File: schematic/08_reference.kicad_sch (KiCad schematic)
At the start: 20 parts, among them U501 OPA4192IDR

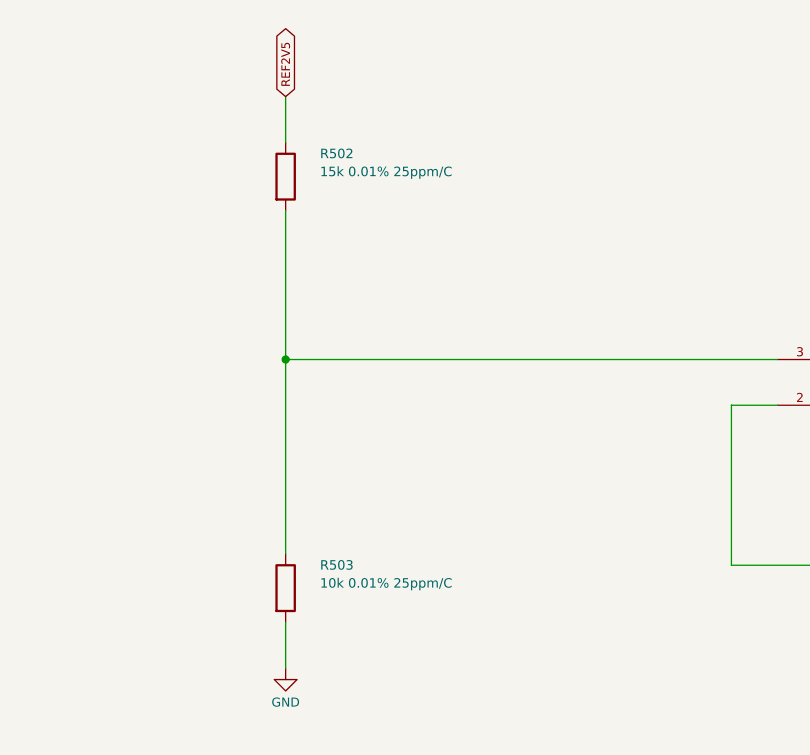
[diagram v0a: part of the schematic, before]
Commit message: add power supply, rail checks and parts list
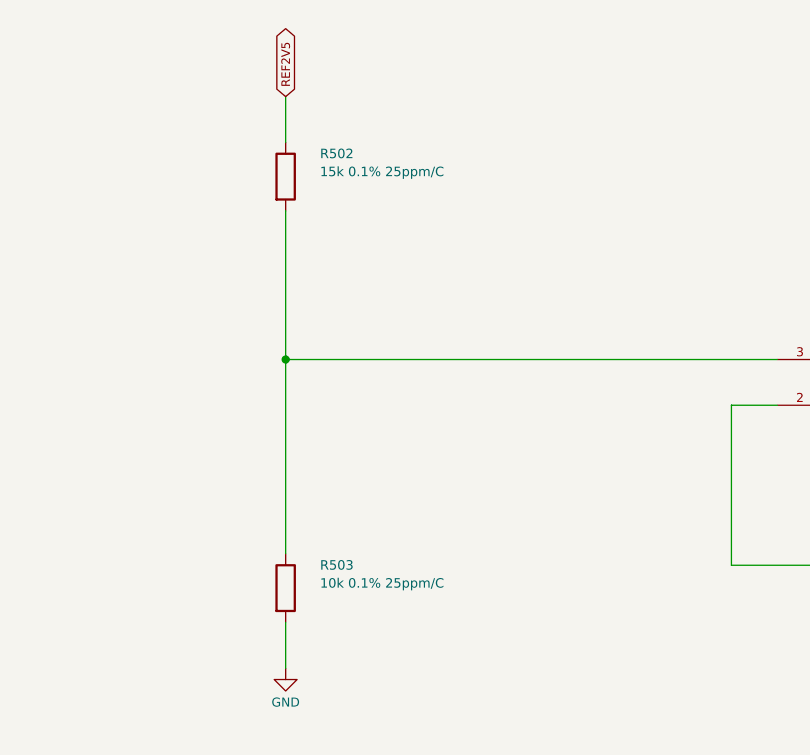
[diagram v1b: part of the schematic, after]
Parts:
- D501: MPN (none) -> LM4040A25IDBZR; Manufacturer (none) -> Texas Instruments; Supplier (none) -> LCSC
- R502: value 15k 0.01% 25ppm/C -> 15k 0.1% 25ppm/C
- R503: value 10k 0.01% 25ppm/C -> 10k 0.1% 25ppm/C
- R504, R505: MPN (none) -> RNCF0805TKY10K0; Manufacturer (none) -> Stackpole; Supplier (none) -> Mouser; Supplier URL (none) -> https://www.mouser.com/ProductDetail/SEI-Stackpole/RNCF0805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
- U501: MPN (none) -> OPA4192IDR; Manufacturer (none) -> Texas Instruments; Supplier (none) -> LCSC; Supplier URL (none) -> https://www.lcsc.com/product-detail/C2057908.html
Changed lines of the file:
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@@
       )
     )
-    (property "Datasheet" "http://www.ti.com/lit/ds/symlink/lm4040-n.pdf"
+    (property "Datasheet" "https://www.ti.com/lit/ds/symlink/lm4040.pdf"
       (at 74.93 64.77000000000001 90.0)
       (effects
         (font
           (size 1.05 1.05)
+        )
+        (hide yes)
+      )
+    )
+    (property "MPN" "LM4040A25IDBZR"
+      (at 74.93 74.93 0.0)
+      (effects
+        (font
+          (size 1.0 1.0)
+        )
+        (hide yes)
+      )
+    )
+    (property "Manufacturer" "Texas Instruments"
+      (at 74.93 74.93 0.0)
+      (effects
+        (font
+          (size 1.0 1.0)
+        )
+        (hide yes)
+      )
+    )
+    (property "Supplier" "LCSC"
+      (at 74.93 74.93 0.0)
+      (effects
+        (font
+          (size 1.0 1.0)
         )
         (hide yes)
@@
       )
     )
-    (property "Value" "15k 0.01% 25ppm/C"
+    (property "Value" "15k 0.1% 25ppm/C"
       (at 158.75 59.15 0.0)
       (effects
@@
       )
     )
-    (property "Value" "10k 0.01% 25ppm/C"
+    (property "Value" "10k 0.1% 25ppm/C"
       (at 158.75 104.86999999999999 0.0)
       (effects
@@
       )
     )
+    (property "MPN" "RNCF0805TKY10K0"
+      (at 299.72 134.62 0.0)
+      (effects
+        (font
+          (size 1.0 1.0)
+        )
+        (hide yes)
+      )
+    )
+    (property "Manufacturer" "Stackpole"
+      (at 299.72 134.62 0.0)
+      (effects
+        (font
+          (size 1.0 1.0)
+        )
+        (hide yes)
+      )
+    )
+    (property "Supplier" "Mouser"
+      (at 299.72 134.62 0.0)
+      (effects
+        (font
+          (size 1.0 1.0)
+        )
+        (hide yes)
+      )
+    )
+    (property "Supplier URL" "https://www.mouser.com/ProductDetail/SEI-Stackpole/RNCF0805TKY10K0?qs=FESYatJ8odKPVkqigBJMsg%3D%3D"
+      (at 299.72 134.62 0.0)
+      (effects
+        (font
+          (size 1.0 1.0)
+        )
+        (hide yes)
+      )
+    )
     (instances
       (project "arpeggiator"
@@
         )
         (justify left)
+        (hide yes)
+      )
+    )
+    (property "MPN" "RNCF0805TKY10K0"
+      (at 359.41 110.49 0.0)
+      (effects
+        (font
+          (size 1.0 1.0)
+        )
+        (hide yes)
+      )
+    )
+    (property "Manufacturer" "Stackpole"
+      (at 359.41 110.49 0.0)
+      (effects
+        (font
+          (size 1.0 1.0)
+        )
+        (hide yes)
+      )
+    )
+    (property "Supplier" "Mouser"
+      (at 359.41 110.49 0.0)
+      (effects
+        (font
+          (size 1.0 1.0)
+        )
+        (hide yes)
+      )
+    )
+    (property "Supplier URL" "https://www.mouser.com/ProductDetail/SEI-Stackpole/RNCF0805TKY10K0?qs=FESYatJ8odKPVkqigBJMsg%3D%3D"
+      (at 359.41 110.49 0.0)
+      (effects
+        (font
+          (size 1.0 1.0)
+        )
         (hide yes)
       )
@@
       )
     )
+    (property "MPN" "OPA4192IDR"
+      (at 219.71 82.55 0.0)
+      (effects
+        (font
+          (size 1.0 1.0)
+        )
+        (hide yes)
+      )
+    )
+    (property "Manufacturer" "Texas Instruments"
+      (at 219.71 82.55 0.0)
+      (effects
+        (font
+          (size 1.0 1.0)
+        )
+        (hide yes)
+      )
+    )
+    (property "Supplier" "LCSC"
+      (at 219.71 82.55 0.0)
+      (effects
+        (font
+          (size 1.0 1.0)
+        )
+        (hide yes)
+      )
+    )
+    (property "Supplier URL" "https://www.lcsc.com/product-detail/C2057908.html"
+      (at 219.71 82.55 0.0)
+      (effects
+        (font
+          (size 1.0 1.0)
+        )
+        (hide yes)
+      )
+    )
     (instances
       (project "arpeggiator"
@@
         )
         (hide yes)
+      )
+    )
+    (property "MPN" "OPA4192IDR"
+      (at 330.2 82.55 0.0)
+      (effects
+        (font
+          (size 1.0 1.0)
+        )
+        (hide yes)
+      )
+    )
+    (property "Manufacturer" "Texas Instruments"
+      (at 330.2 82.55 0.0)
+      (effects
+        (font
+          (size 1.0 1.0)
+        )
+        (hide yes)
+      )
+    )
+    (property "Supplier" "LCSC"
+      (at 330.2 82.55 0.0)
+      (effects
+        (font
+          (size 1.0 1.0)
+        )
+        (hide yes)
+      )
+    )
+    (property "Supplier URL" "https://www.lcsc.com/product-detail/C2057908.html"
+      (at 330.2 82.55 0.0)
+      (effects
+        (font
+          (size 1.0 1.0)
+        )
+        (hide yes)
